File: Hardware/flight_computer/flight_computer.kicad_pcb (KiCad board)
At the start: 4 copper layers, 80 x 100 mm, 125 parts, among them J1 Micro_USB, J10 Conn_02x01, J2 MicroSD_molex, J3 rpi_zero_w, J4 JST_8_RA, J5 JST_GH_6_RA, J6 JST_GH_4_RA, J7 JST_GH_5_RA, J8 Conn_02x03, J9 Conn_02x03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

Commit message: fixed issue with plane overlapping. Added new centroid and gerber files
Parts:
- removed G***: LOGO, drone_footprints:osprey_bitmap2
- removed G***: LOGO, drone_footprints:osprey_bitmap3
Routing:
- net GND: vias 152 -> 154

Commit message: fixed issue with RC connector. Try again tomorrow
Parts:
- added G***: LOGO, drone_footprints:osprey_bitmap2, B.Cu at (124.1, 107.1)
- added G***: LOGO, drone_footprints:osprey_bitmap3, F.Cu at (97.0, 89.9)
- moved R12 4.06 mm to (151.6, 119.2)
- moved R11 0.57 mm to (151.6, 117.3)
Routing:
- net GND: track 250.2 -> 246.5 mm, vias 154 -> 155
- net /CONNECTORS/rc_in: track 12.1 -> 8.85 mm
- net /VDD_3V3_RADIO: track 8.90 -> 12.1 mm, vias 0 -> 2
- net Net-(R12-Pad2): track 6.43 -> 4.16 mm, vias 2 -> 0

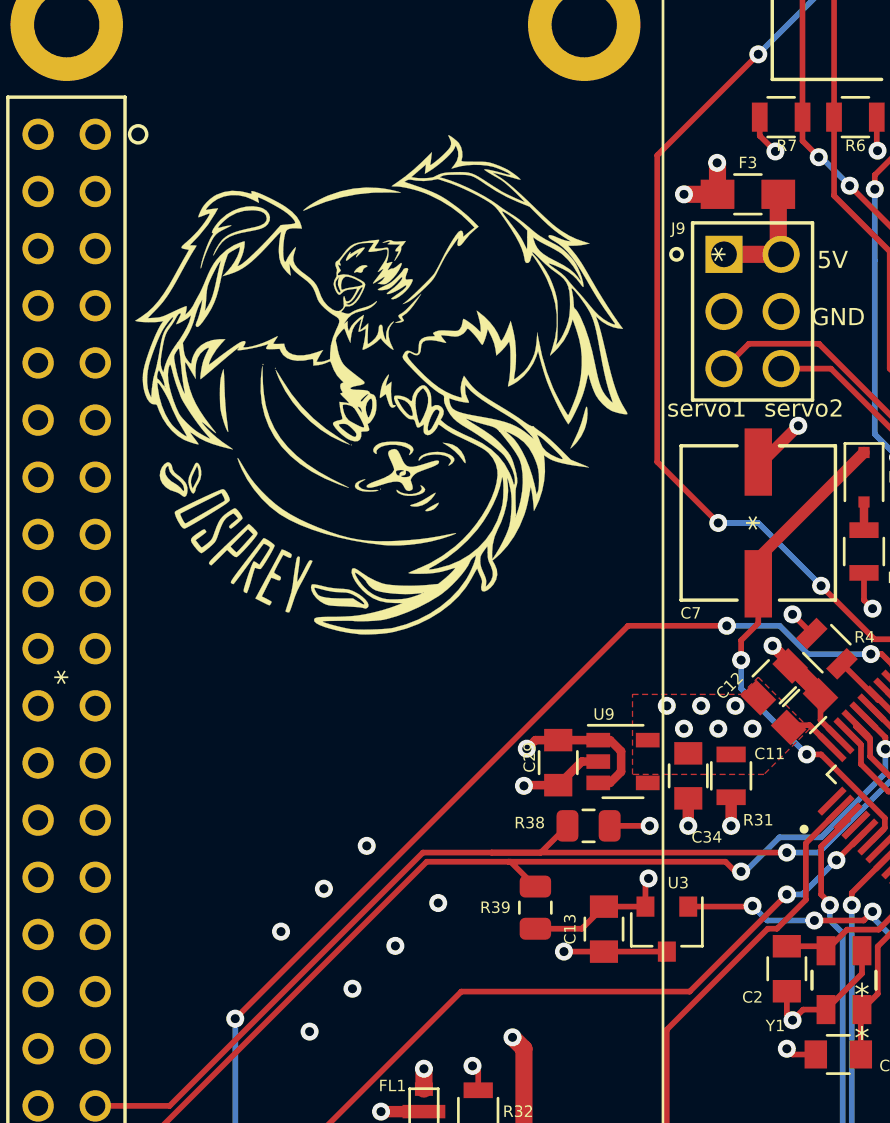
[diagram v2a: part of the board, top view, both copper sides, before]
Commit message: Fixes watchdog on layout
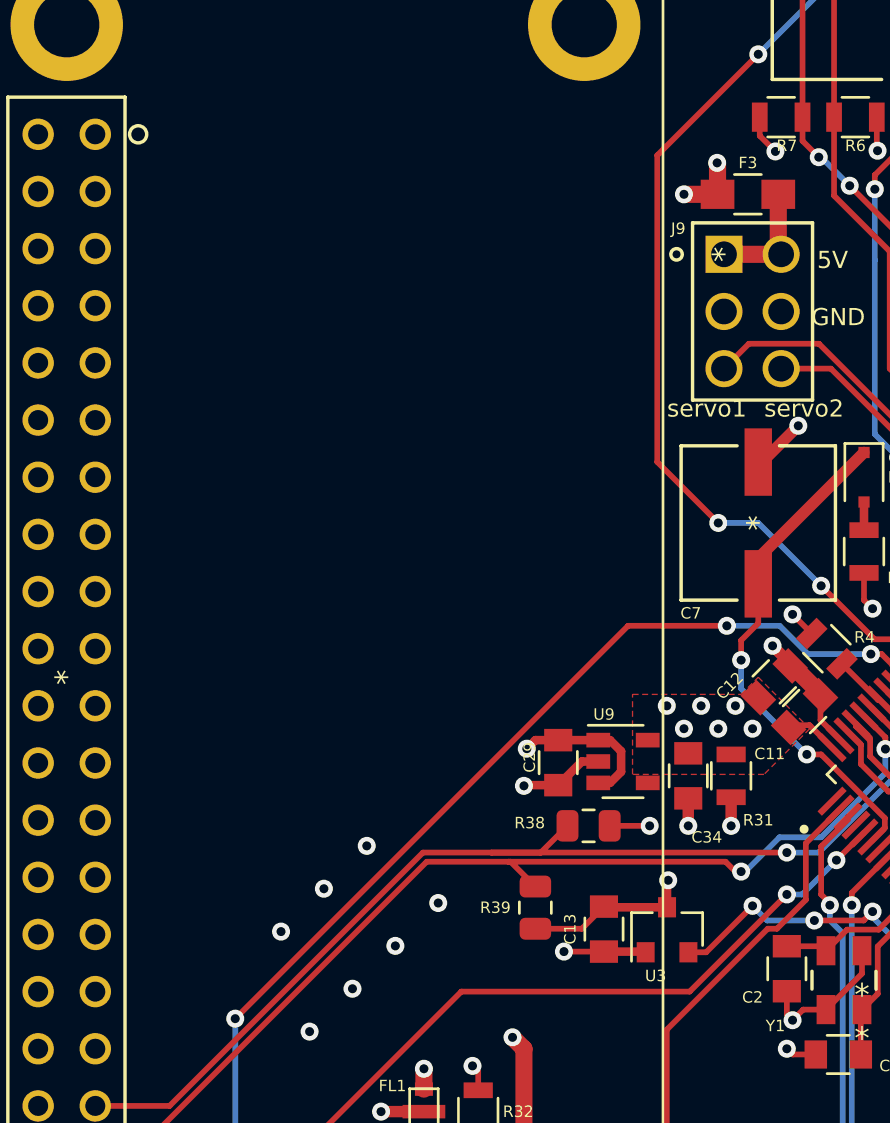
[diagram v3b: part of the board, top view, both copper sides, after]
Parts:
- removed G***: LOGO, drone_footprints:osprey_bitmap2
- removed G***: LOGO, drone_footprints:osprey_bitmap3
- turned U3 to 90 degrees
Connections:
- U3 pad 1: /~RST -> GND
- U3 pad 2: /VDD_3V3_STM -> /~RST
- U3 pad 3: GND -> /VDD_3V3_STM
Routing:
- net GND: track 246.5 -> 245.6 mm
- net /VDD_3V3_STM: track 165.2 -> 166.1 mm
- net /~RST: track 13.3 -> 14.2 mm

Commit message: Updates RC layout
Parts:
- moved R30 15.2 mm to (144.6, 109.4), turned to 90 degrees
- moved C27 14.0 mm to (152.0, 110.2), turned to 0 degrees
- moved U7 11.4 mm to (147.8, 111.7), turned to 270 degrees
- moved C32 8.77 mm to (152.2, 114.8), turned to 90 degrees
- moved C30 8.73 mm to (150.3, 114.8), turned to 90 degrees
- moved R11 1.21 mm to (151.1, 118.4)
- moved R12 1.21 mm to (151.1, 120.3)
- moved U4 1.21 mm to (146.8, 118.3)
- moved D8 1.20 mm to (151.8, 107.3)
- moved D9 1.20 mm to (151.8, 104.2)
- moved R10 1.20 mm to (155.4, 107.3)
- moved R27 1.20 mm to (155.4, 104.2)
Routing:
- net /VDD_3V3_RADIO_EN: track 19.5 -> 25.5 mm
- net /VDD_3V3_RADIO: track 12.1 -> 7.75 mm, vias 2 -> 0
- net /CONNECTORS/rc_in: track 8.85 -> 10.3 mm
- net /DEBUG_LED_2: track 23.1 -> 21.9 mm
- net /VDD_3V3_STM: track 166.1 -> 167.3 mm, vias 32 -> 33
- net /DEBUG_LED_1: track 23.8 -> 22.7 mm
- net /RC_INPUT_USART1_RX: track 32.5 -> 33.5 mm
- net /VDD_5V_IN: track 21.7 -> 20.8 mm
- net GND: track 245.6 -> 246.4 mm
- net Net-(J7-Pad3): track 2.00 -> 2.82 mm

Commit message: added new gerber files
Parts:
- added G***: LOGO, drone_footprints:osprey_bitmap2, B.Cu at (123.1, 107.8)
- added G***: LOGO, drone_footprints:osprey_bitmap3, F.Cu at (97.2, 89.4)

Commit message: Adds updated gerbers
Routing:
- net GND: track 246.4 -> 253.9 mm, vias 155 -> 157
- net /VDD_5V_IN: track 20.8 -> 22.3 mm, vias 14 -> 15
- net /VDD_3V3_STM: track 167.3 -> 168.4 mm

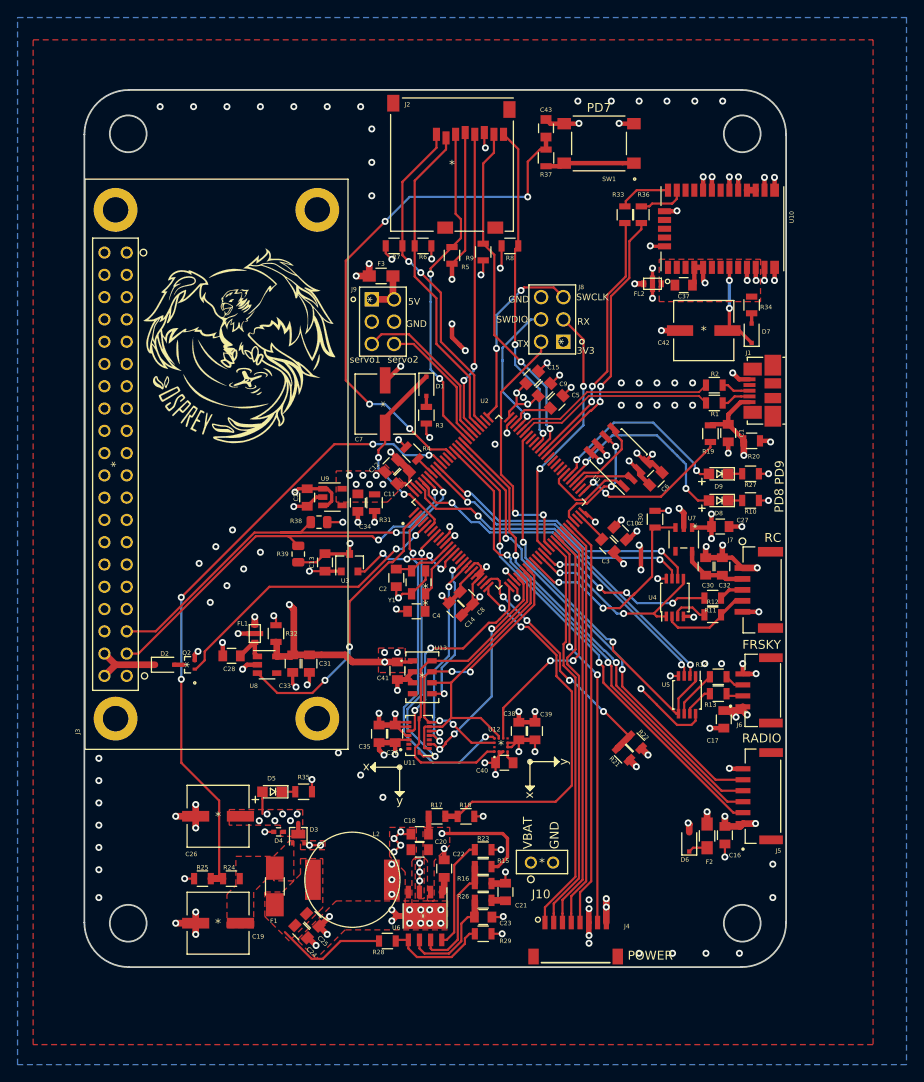
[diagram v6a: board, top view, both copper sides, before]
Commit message: added more 3d components
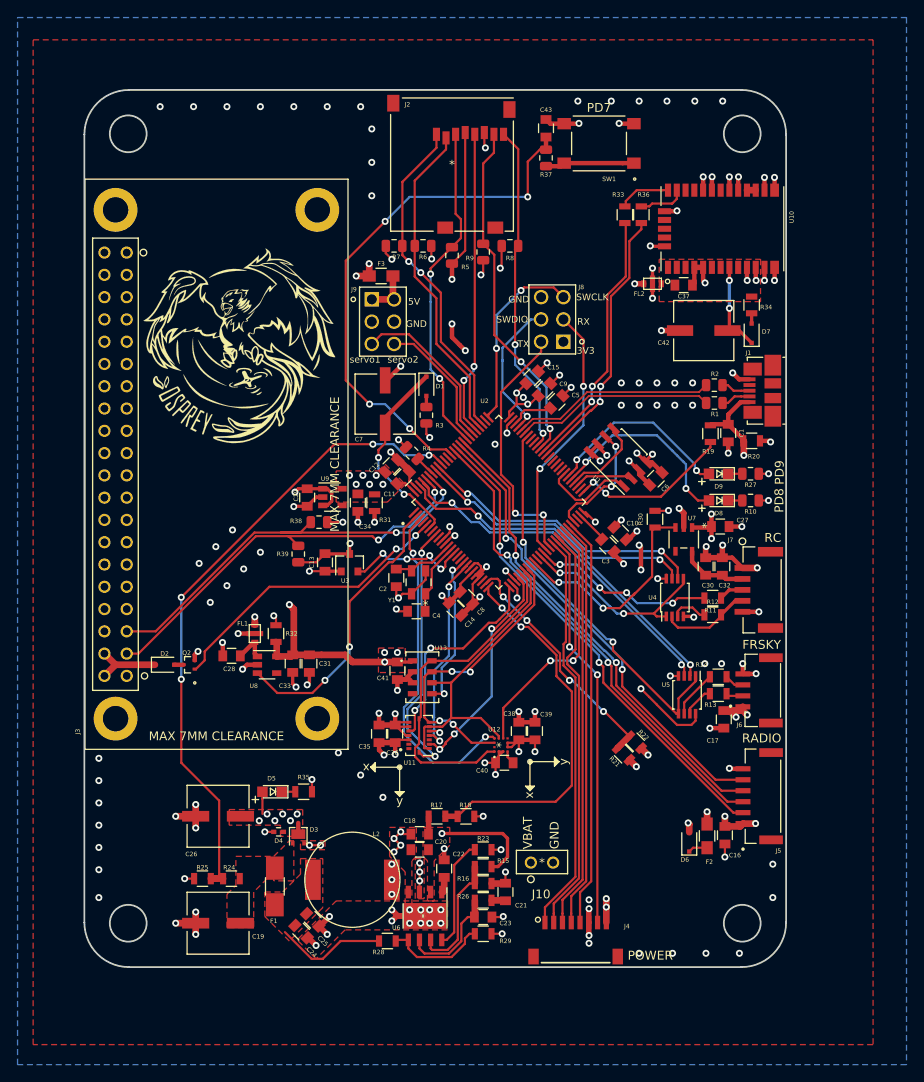
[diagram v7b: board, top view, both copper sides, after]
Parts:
- C1, C10, C11, C12, C13, C14, C15, C2, C3, C4, C43, C5, C6, C8, C9: footprint Capacitors_SMD:C_0805 -> drone_footprints:C_0805
- R1, R10, R2, R27, R3, R37, R4, R5, R6, R7, R8, R9: footprint Resistors_SMD:R_0805 -> drone_footprints:R_0805
- U3: footprint TO_SOT_Packages_SMD:SOT-23 -> drone_footprints:SOT-23
